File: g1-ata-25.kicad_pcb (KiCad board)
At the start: 2 copper layers, 81.3 x 130.4 mm, 37 parts, among them P1 G1_DC_SOCKET, P2 G1_GD_PLUGNH, P3 IDE_40PIN, P4 IDE_44PIN, P5 CONN_01X02, P6 CONN_01X04, P7 CONN_01X04, P8 CONN_01X05, U1 TCXO_DFAS11, U2 TS30011-M050

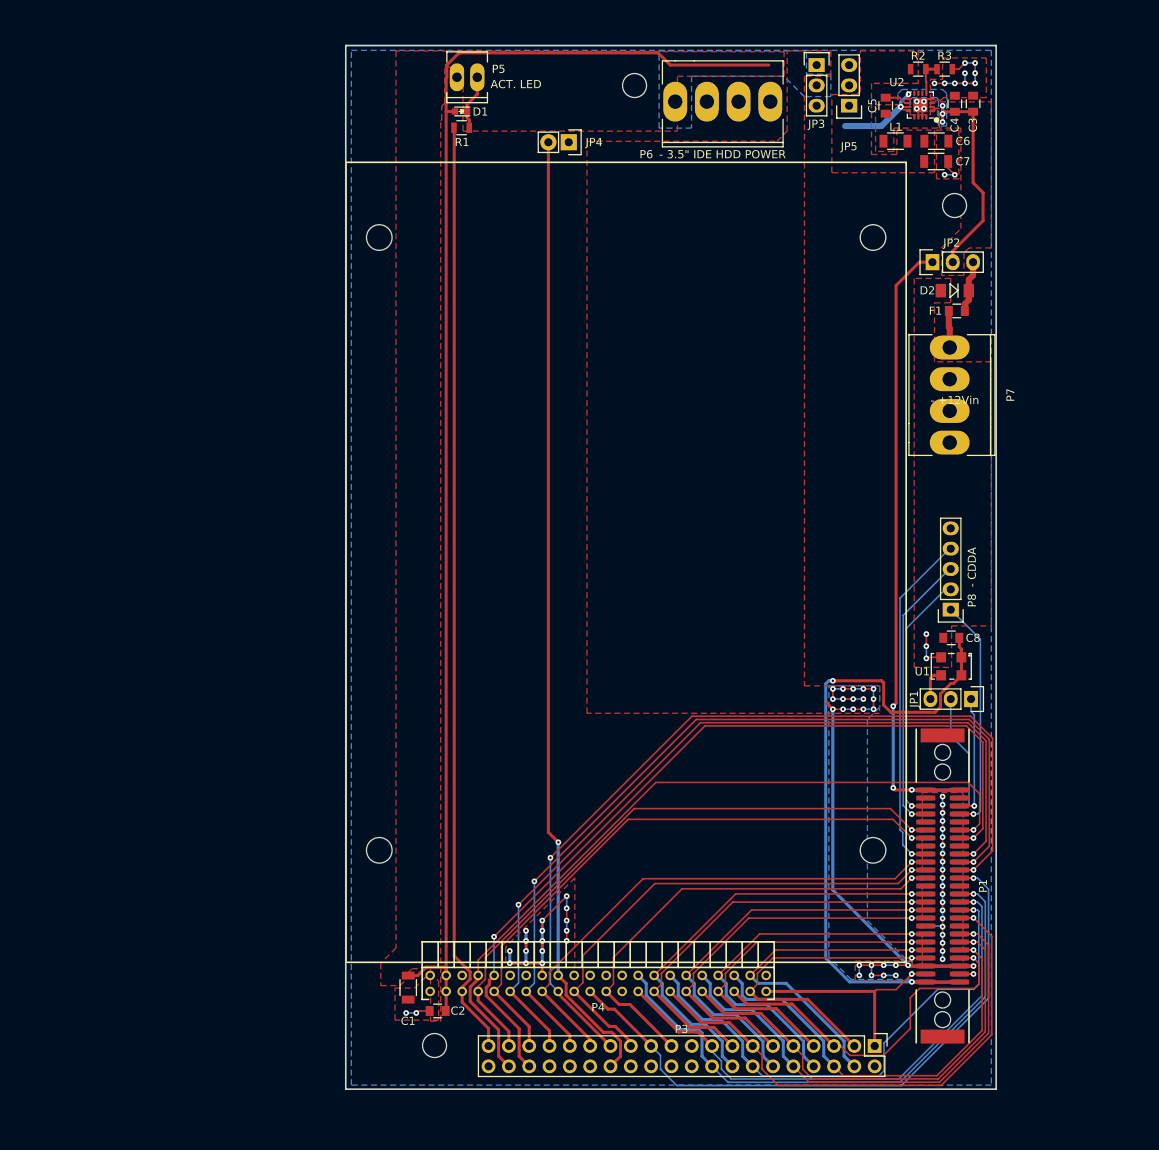
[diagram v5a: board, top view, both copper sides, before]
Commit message: Added fuse + polarity protection for 5V input (not yet routed).
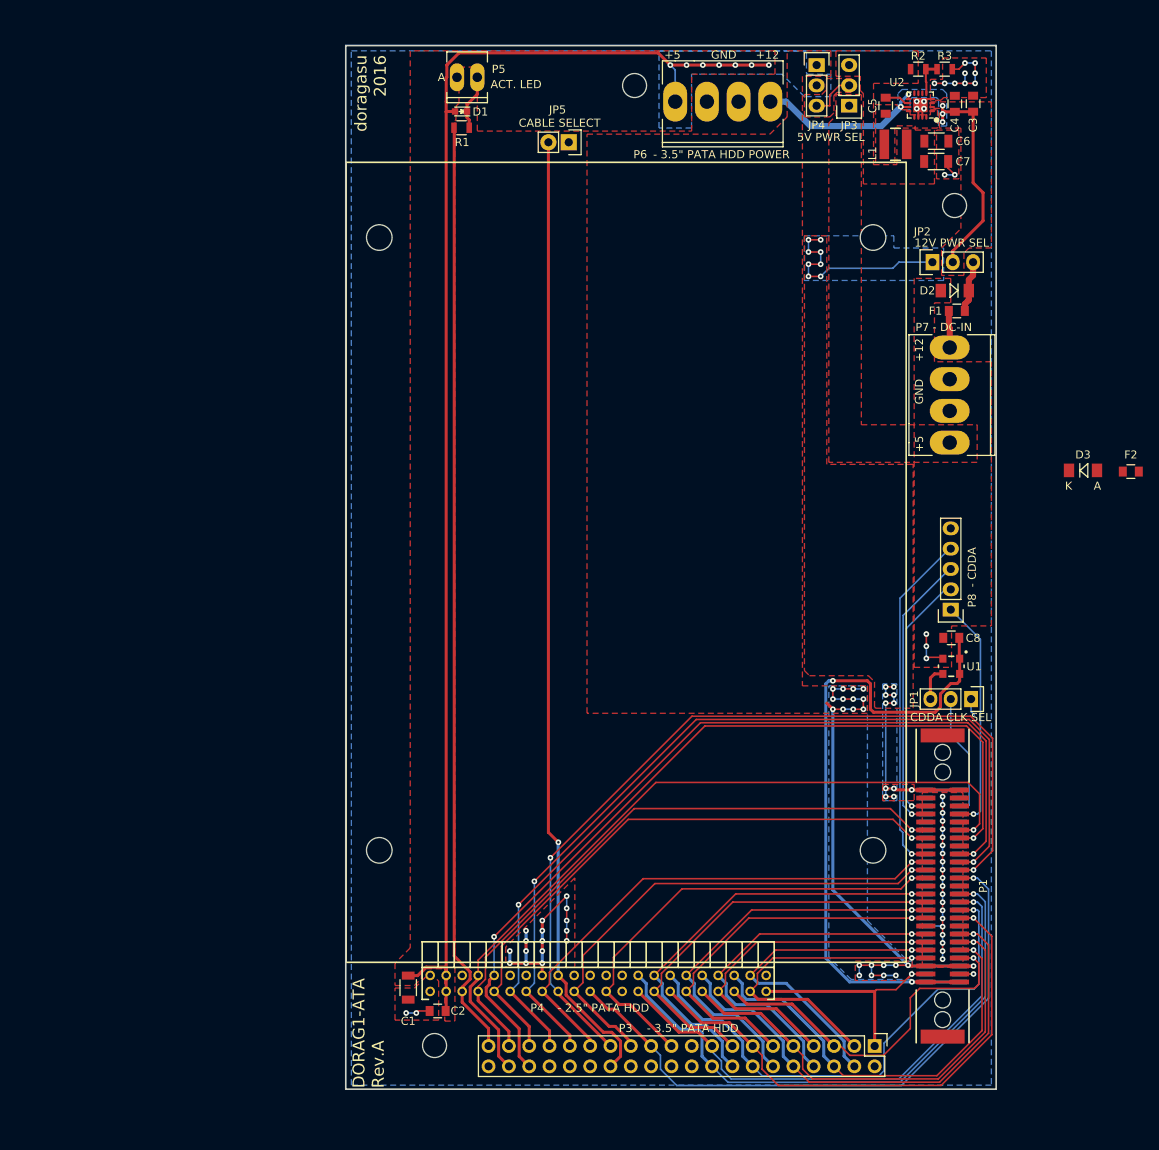
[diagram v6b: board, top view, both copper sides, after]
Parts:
- added D3: D, Diodes_SMD:MiniMELF_Standard, F.Cu at (211.6, 72.5)
- added F2: F_Small, Capacitors_SMD:C_0805, F.Cu at (217.6, 72.7)
- L1: footprint Capacitors_SMD:C_1206 -> doragasu:INDUCTOR-NR4018
- U1: value TCXO_DFAS11 -> DSC1001; footprint doragasu:OSC_F530L -> doragasu:DSC1001-32x25M
- moved L1 0.40 mm to (188.2, 31.8)
- renumbered JP5 to JP3, JP3 to JP4, JP4 to JP5
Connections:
- JP1 pad 1: Net-(JP1-Pad1) -> GND
- JP3 pad 1: Net-(JP5-Pad1) -> Net-(D3-Pad1)
- P1 pad B23: Net-(JP1-Pad1) -> Net-(P1-PadB23)
- P7 pad 4: Net-(JP5-Pad1) -> Net-(F2-Pad1)
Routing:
- net +12P: track 83.0 -> 59.8 mm, vias 3 -> 19
- net +5V: track 167.7 -> 184.8 mm, vias 0 -> 7
- net Net-(JP1-Pad1): track 15.4 -> 0.00 mm, vias 1 -> 0
- net +12V: track 39.4 -> 50.0 mm
- net Net-(JP3-Pad2): track 0.00 -> 6.06 mm
- net +5VP: track 82.9 -> 79.1 mm, vias 25 -> 22
- net GND: track 75.6 -> 77.7 mm
- added copper zone on B.Cu, net +12P
- added copper zone on F.Cu, net +12P
- added copper zone on F.Cu, net Net-(D3-Pad1)
- added copper zone on F.Cu, net Net-(JP3-Pad2)
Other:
- board text added: "+12"
- board text added: "+5"
- board text added: "- 2.5" PATA HDD"
- board text added: "- 3.5" PATA HDD"
- board text added: "- 3.5" PATA HDD POWER"
- board text added: "- DC-IN"
- board text added: "12V PWR SEL"
- board text added: "5V PWR SEL"
- board text added: "A"
- board text added: "CABLE SELECT"
- board text added: "CDDA CLK SEL"
- board text added: "DORAG1-ATA Rev.A"
- board text added: "GND"
- board text added: "doragasu 2016"
- board text removed: "- +12Vin"
- board text removed: "- 3.5" IDE HDD POWER"
- board text removed: "- Check oscillator pinout. - Check inductor footprint. - Check fuse pinout."

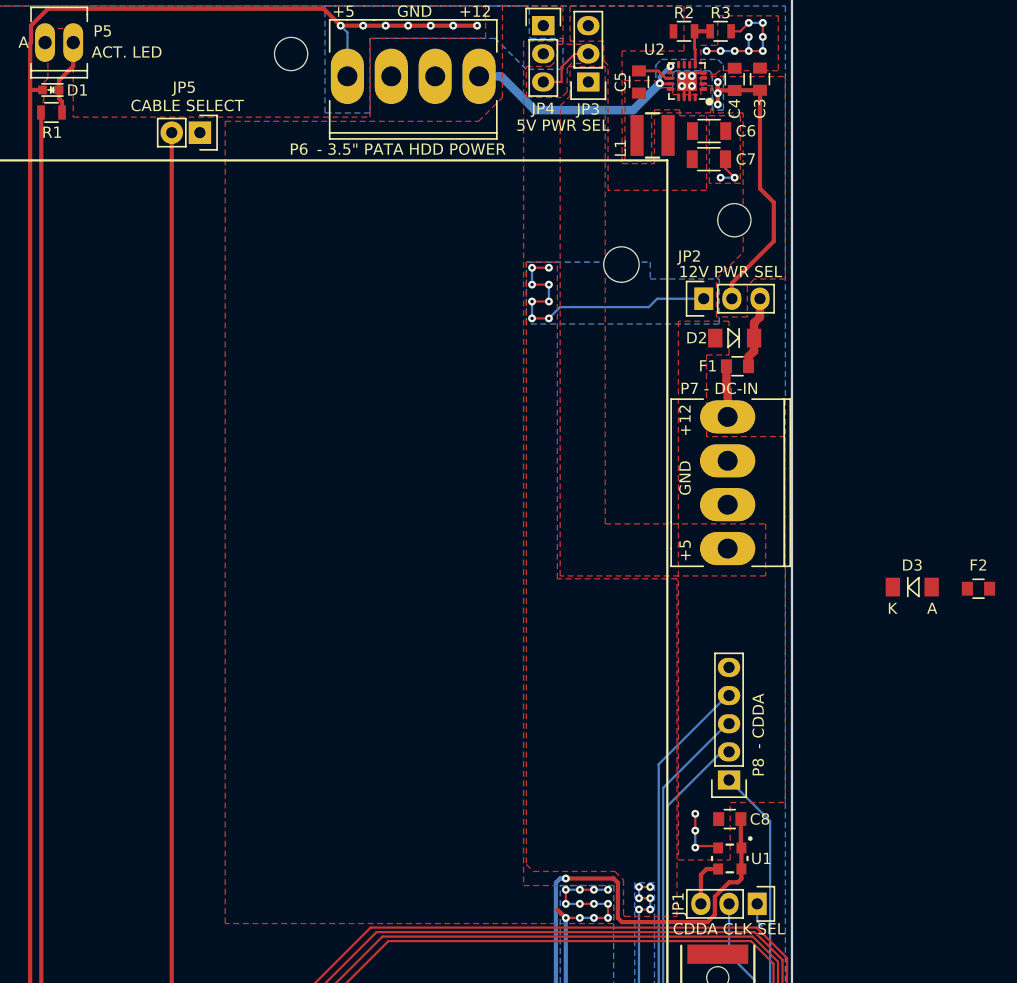
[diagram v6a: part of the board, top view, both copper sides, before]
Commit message: Added jumper settings tables on silk screen.
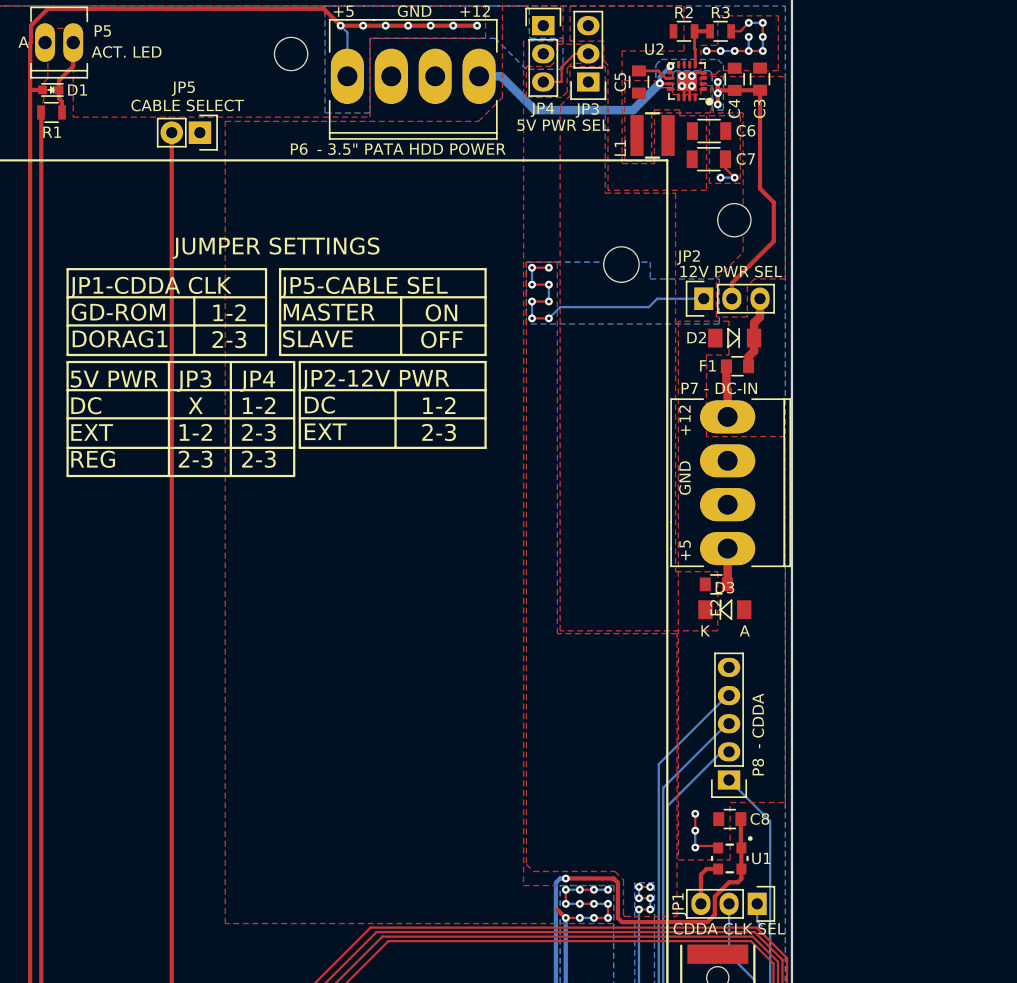
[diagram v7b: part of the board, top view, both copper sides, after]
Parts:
- moved F2 23.7 mm to (193.9, 72.3), turned to 180 degrees
- moved D3 17.0 mm to (194.7, 74.5)
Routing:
- net Net-(F2-Pad1): track 0.00 -> 3.24 mm
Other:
- board text added: "1-2 2-3"
- board text added: "5V PWR DC EXT REG"
- board text added: "JP1-CDDA CLK GD-ROM DORAG1"
- board text added: "JP2-12V PWR DC EXT"
- board text added: "JP3 X 1-2 2-3"
- board text added: "JP4 1-2 2-3 2-3"
- board text added: "JP5-CABLE SEL MASTER SLAVE"
- board text added: "JUMPER SETTINGS"
- board text added: "ON OFF"

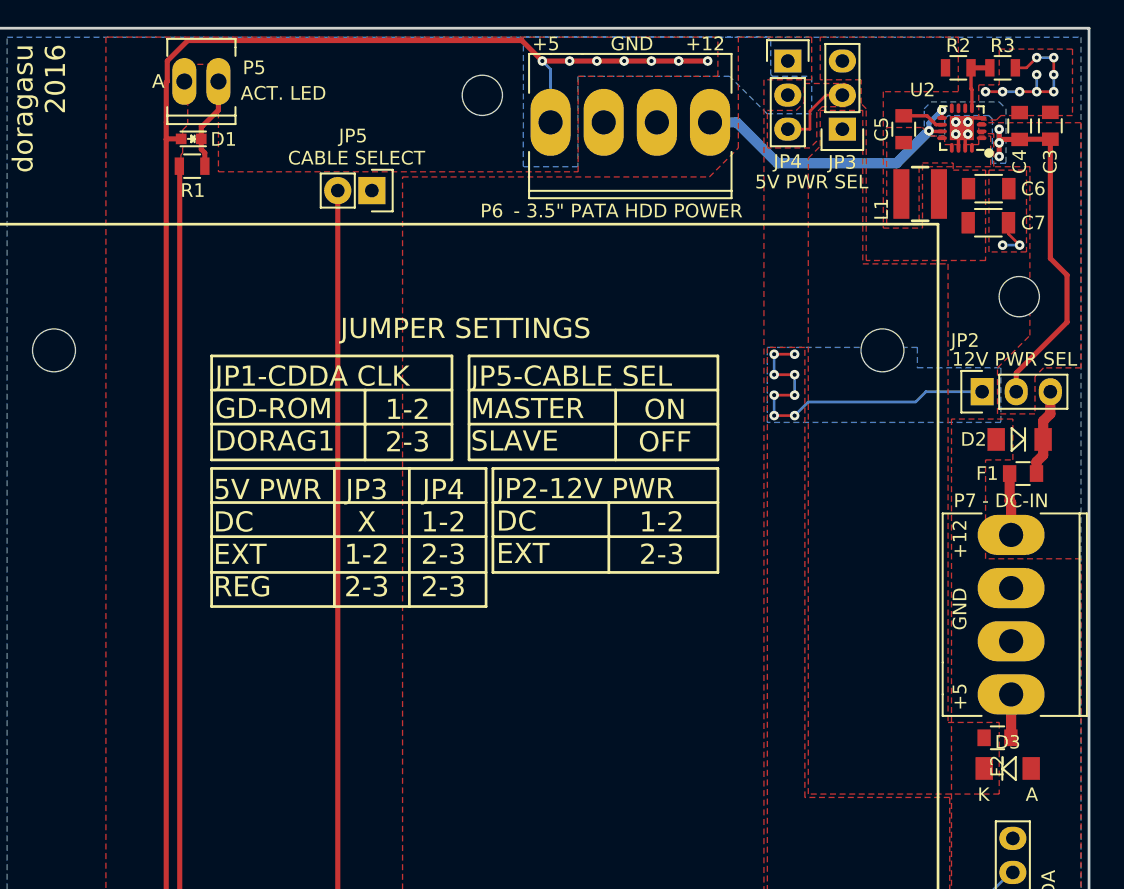
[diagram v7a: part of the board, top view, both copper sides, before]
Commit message: Added OSHW symbol and some more tiny teaks to silk screen.
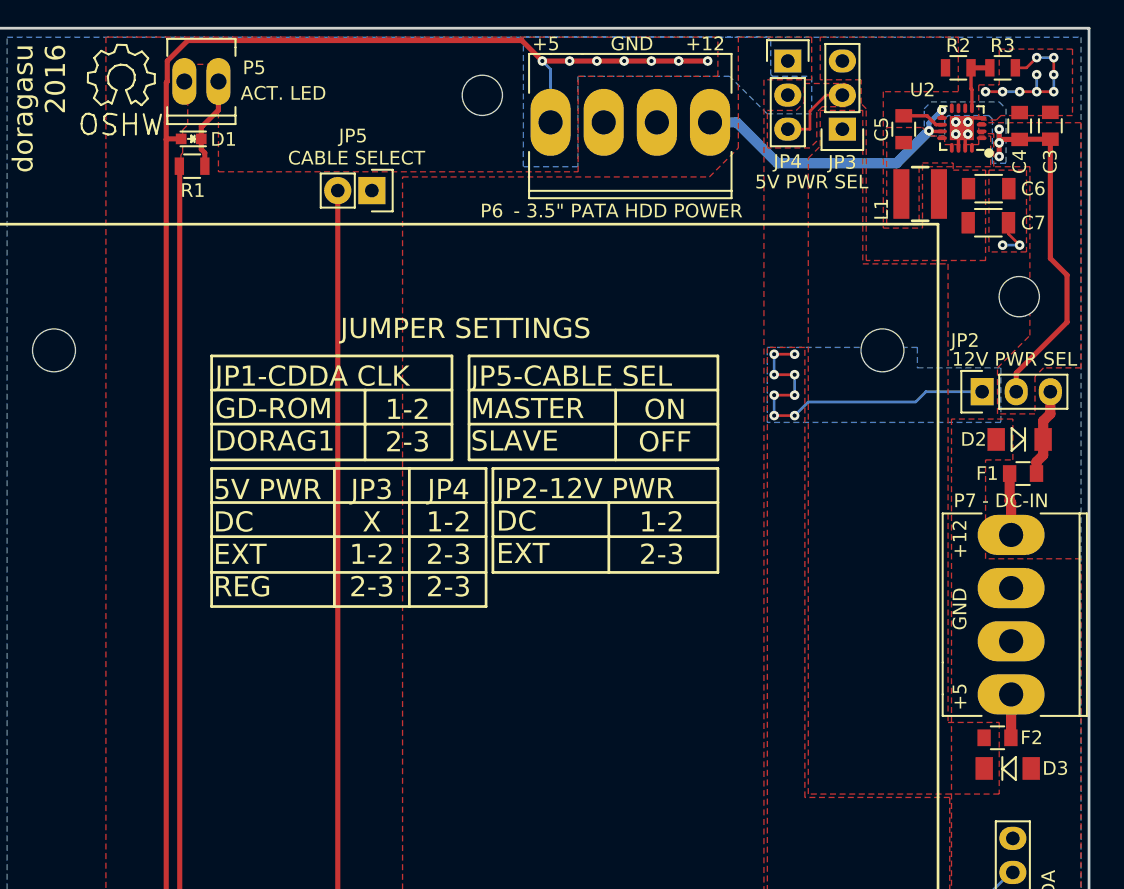
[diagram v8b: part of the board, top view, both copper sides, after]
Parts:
- added Symbol_OSHW-Logo_SilkScreen: VAL**, Symbols:Symbol_OSHW-Logo_SilkScreen, F.Cu at (128.7, 23.1)
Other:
- board text removed: "A"
